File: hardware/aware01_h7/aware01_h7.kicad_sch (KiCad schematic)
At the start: 15 parts, among them U12 STM32H7B0ZBTx, U15 IS45S16800F-7TLA2, Y2 Crystal_GND24

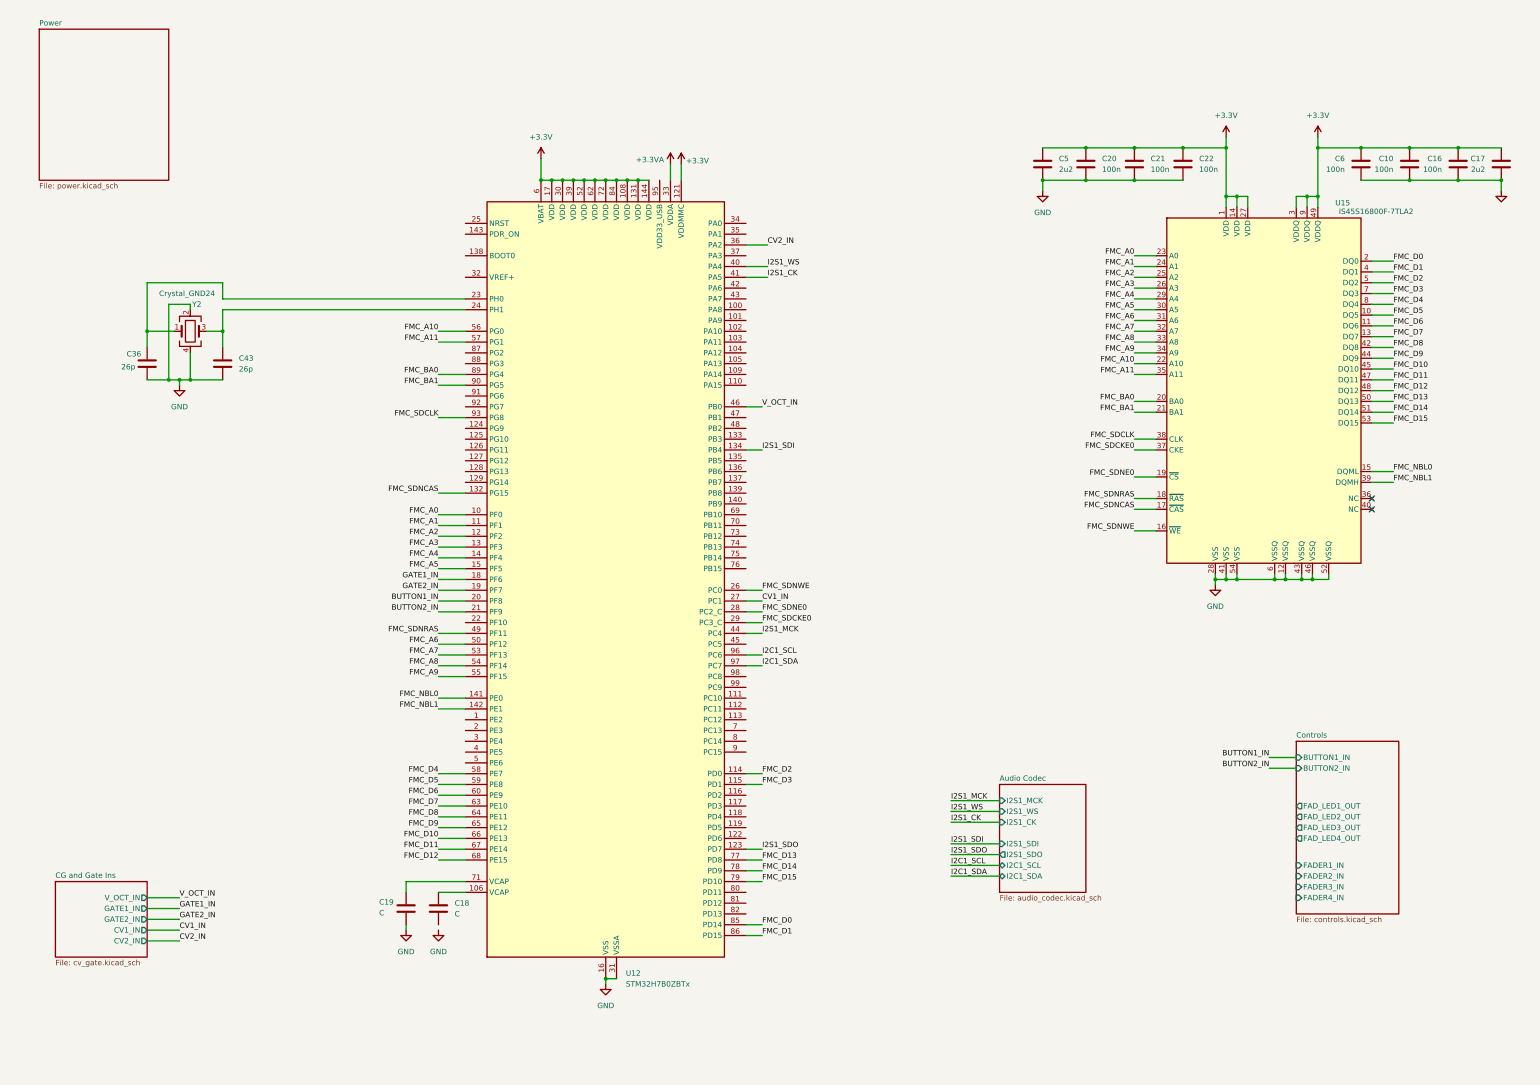
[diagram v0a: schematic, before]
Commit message: update schematic
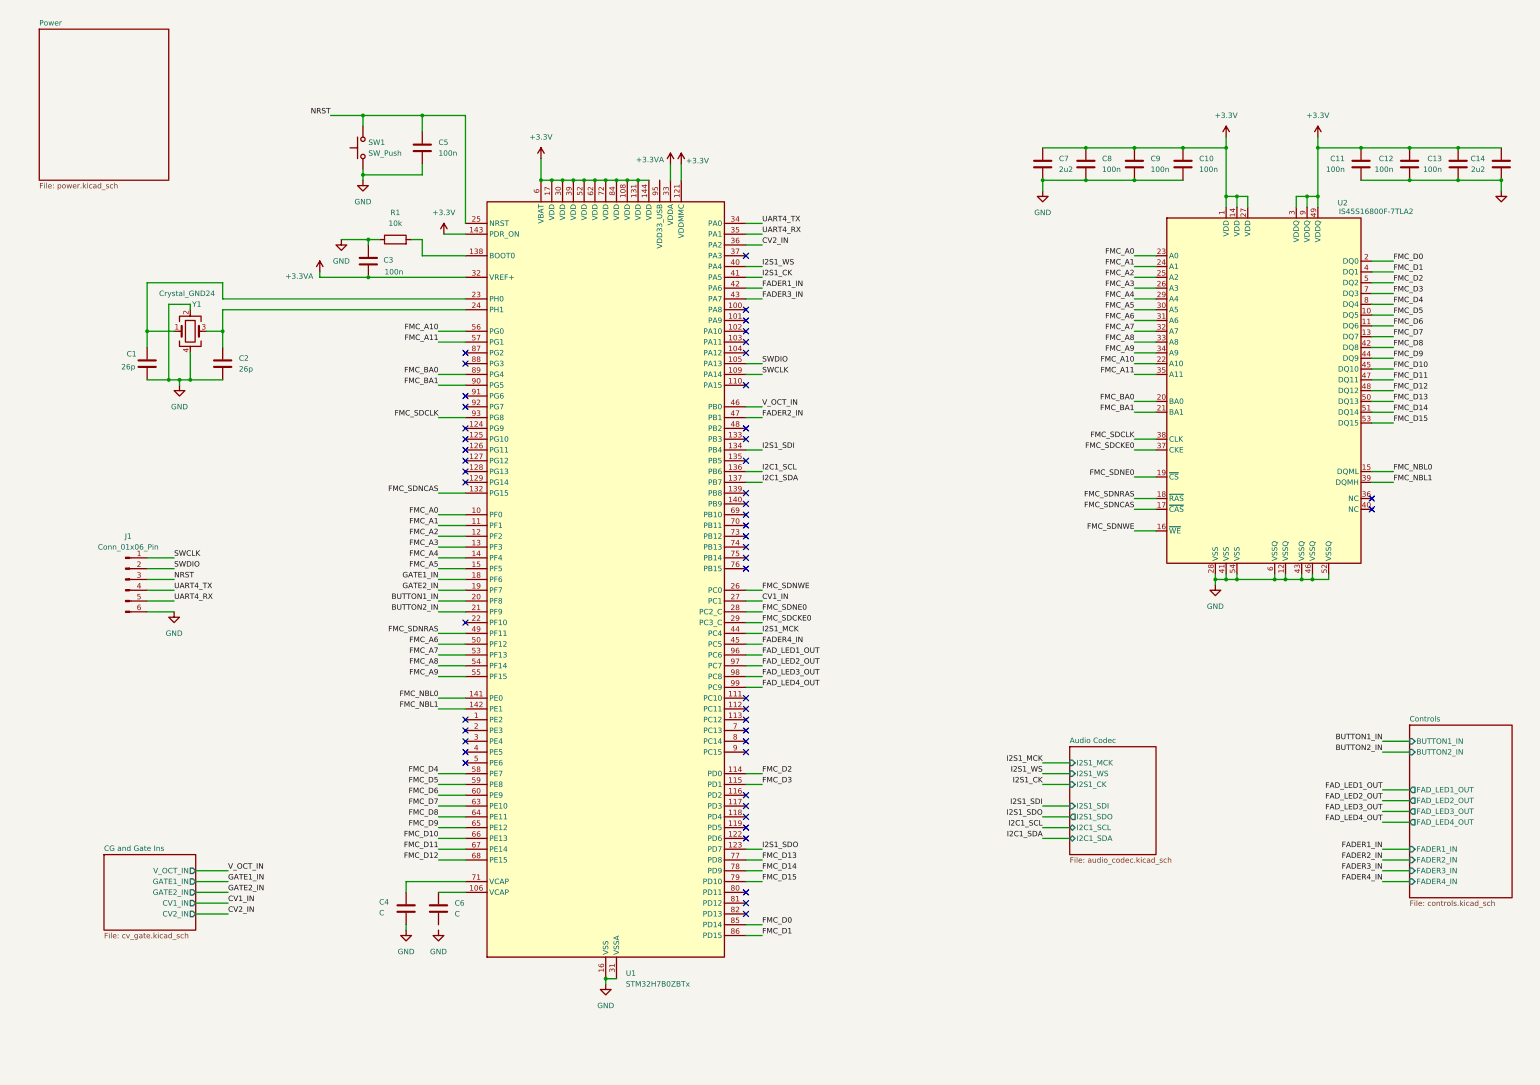
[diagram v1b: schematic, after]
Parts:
- added C3: 100n, symbol Device:C
- added C5: 100n, Capacitor_SMD:C_0201_0603Metric, symbol Device:C
- added J1: Conn_01x06_Pin, symbol Connector:Conn_01x06_Pin
- added R1: 10k, symbol Device:R
- added SW1: SW_Push, symbol Switch:SW_Push
- renumbered C36 to C1, C22 to C10, C6 to C11, C10 to C12, C16 to C13, C17 to C14, C43 to C2, C19 to C4, C18 to C6, C5 to C7, C20 to C8, C21 to C9, U12 to U1, U15 to U2, Y2 to Y1
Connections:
- net +3.3V: now also U1.143 (PDR_ON)
- net +3.3VA: now also U1.32 (VREF+), C3.2
- net GND: now also C3.1, C5.2, J1.6 (Pin_6), R1.1, SW1.1
- net I2C1_SCL: now also U1.136 (PB6); no longer U1.96 (PC6)
- net I2C1_SDA: now also U1.137 (PB7); no longer U1.97 (PC7)
- net SWDIO: now reaches U1.105 (PA13)
- net SWDIO: now also J1.2 (Pin_2)
- net SWCLK: now reaches U1.109 (PA14)
- net SWCLK: now also J1.1 (Pin_1)
- net at U1.138 (BOOT0): now also R1.2
- net NRST: now reaches U1.25 (NRST)
- net NRST: now also C5.1, J1.3 (Pin_3), SW1.2
- net UART4_TX: now reaches U1.34 (PA0)
- net UART4_TX: now also J1.4 (Pin_4)
- net UART4_RX: now reaches U1.35 (PA1)
- net UART4_RX: now also J1.5 (Pin_5)
- net FADER1_IN: now reaches U1.42 (PA6)
- net FADER3_IN: now reaches U1.43 (PA7)
- net FADER4_IN: now reaches U1.45 (PC5)
- net FADER2_IN: now reaches U1.47 (PB1)
- net FAD_LED3_OUT: now reaches U1.98 (PC8)
- net FAD_LED4_OUT: now reaches U1.99 (PC9)
- new net FAD_LED1_OUT: U1.96 (PC6)
- new net FAD_LED2_OUT: U1.97 (PC7)
- no-connect marks 2 -> 50

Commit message: refine schematic
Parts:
- C1, C10, C11, C12, C13, C2, C3, C8, C9: footprint (none) -> Capacitor_SMD:C_0603_1608Metric
- C14, C7: value 2u2 -> 2.2u; footprint (none) -> Capacitor_SMD:C_0603_1608Metric
- C4, C6: value C -> 100n; footprint (none) -> Capacitor_SMD:C_0603_1608Metric
- C5: footprint Capacitor_SMD:C_0201_0603Metric -> Capacitor_SMD:C_0603_1608Metric
- J1: footprint (none) -> Connector_PinHeader_2.54mm:PinHeader_1x06_P2.54mm_Vertical
- R1: footprint (none) -> Resistor_SMD:R_0603_1608Metric_Pad0.98x0.95mm_HandSolder
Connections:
- net +3.3V: now also J1.1 (Pin_1), U1.95 (VDD33_USB)
- net GND: now also C6.1
- net NRST: now also J1.5 (Pin_5); no longer J1.3 (Pin_3)
- net SWCLK: now also J1.2 (Pin_2); no longer J1.1 (Pin_1)
- net SWDIO: now also J1.3 (Pin_3); no longer J1.2 (Pin_2)
- net UART4_RX: no longer J1.5 (Pin_5)
- net UART4_TX: no longer J1.4 (Pin_4)
- new net SWO: J1.4 (Pin_4)
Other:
- note added: "BERECHNUNG?"
- note added: "TESTPADS EINBAUEN"
- note added: "TODO: SWO in CubeMX und an MCU in schematic hinzufügen"
- moved on the sheet: C3, C5, R1, SW1

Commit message: assign footprints
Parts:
- added H1, H2, H3, H4: MountingHole, MountingHole:MountingHole_2.2mm_M2_DIN965_Pad_TopOnly, symbol Mechanical:MountingHole
- added J2: Conn_01x03_Pin, symbol Connector:Conn_01x03_Pin
- C1, C2: value 26p -> 22p
- SW1: footprint (none) -> Button_Switch_SMD:SW_Push_1P1T_NO_CK_PTS125Sx43PSMTR
- U2: footprint Eurorack:SOP80P1176X120-54N -> Eurorack:IS45S16800F-7TLA2
- Y1: value Crystal_GND24 -> WE-XTAL 24.0MHz 50ppm; footprint (none) -> Crystal:Crystal_SMD_3225-4Pin_3.2x2.5mm_HandSoldering
- renumbered C5 to C4, C4 to C5
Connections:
- net GND: now also J2.3 (Pin_3)
- net SWO: now also U1.133 (PB3)
- net UART4_RX: now also J2.2 (Pin_2)
- net UART4_TX: now also J2.1 (Pin_1)
- no-connect marks 50 -> 47
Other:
- note removed: "BERECHNUNG?"
- moved on the sheet: C1, C2

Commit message: change jack symbols
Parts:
- J2: footprint (none) -> Connector:FanPinHeader_1x03_P2.54mm_Vertical
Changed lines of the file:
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@@
 			)
 		)
-		(property "Footprint" ""
+		(property "Footprint" "Connector:FanPinHeader_1x03_P2.54mm_Vertical"
 			(at 49.53 182.88 0)
 			(effects

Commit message: update pcb
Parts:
- removed H1, H2, H3, H4: MountingHole, MountingHole:MountingHole_2.2mm_M2_DIN965_Pad_TopOnly, symbol Mechanical:MountingHole
- added C61: 100n, Capacitor_SMD:C_0603_1608Metric, symbol Device:C
- C1, C2: Manufacturer_Name (none) -> KEMET; Manufacturer_Part_Number (none) -> C0603C220J1GACTU; Mouser Part Number (none) -> 80-C0603C220J1G
- C10, C11, C12, C13, C3, C4, C5, C6, C8, C9: Manufacturer_Name (none) -> KYOCERA AVX; Manufacturer_Part_Number (none) -> KAF15BR72A104KT; Mouser Part Number (none) -> 581-KAF15BR72A104KT
- C14, C7: Manufacturer_Name (none) -> Samsung Electro-Mechanics; Manufacturer_Part_Number (none) -> CL10A225KP8NNWC; Mouser Part Number (none) -> 187-CL10A225KP8NNWC
- J2: footprint Connector:FanPinHeader_1x03_P2.54mm_Vertical -> Connector_PinHeader_2.54mm:PinHeader_1x03_P2.54mm_Vertical
- SW1: footprint Button_Switch_SMD:SW_Push_1P1T_NO_CK_PTS125Sx43PSMTR -> Eurorack:TS046643BK100SMT; Manufacturer_Name (none) -> Same Sky; Manufacturer_Part_Number (none) -> TS04-66-43-BK-100-SMT; Mouser Part Number (none) -> 179-TS046643BK100SMT
- U1: Manufacturer_Name (none) -> STMicroelectronics; Manufacturer_Part_Number (none) -> STM32H7B0ZBT6; Mouser Part Number (none) -> 511-STM32H7B0ZBT6
- U2: footprint Eurorack:IS45S16800F-7TLA2 -> Eurorack:SOP80P1176X120-54N; Manufacturer_Name (none) -> ISSI; Manufacturer_Part_Number (none) -> IS45S16800F-7TLA2; Mouser Part Number (none) -> 870-IS45S16800F7TLA2
- Y1: Manufacturer_Name (none) -> Wurth Elektronik; Manufacturer_Part_Number (none) -> 830064703; Mouser Part Number (none) -> 710-830064703
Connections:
- net +3.3VA: now also C61.1
- net GND: now also C61.2

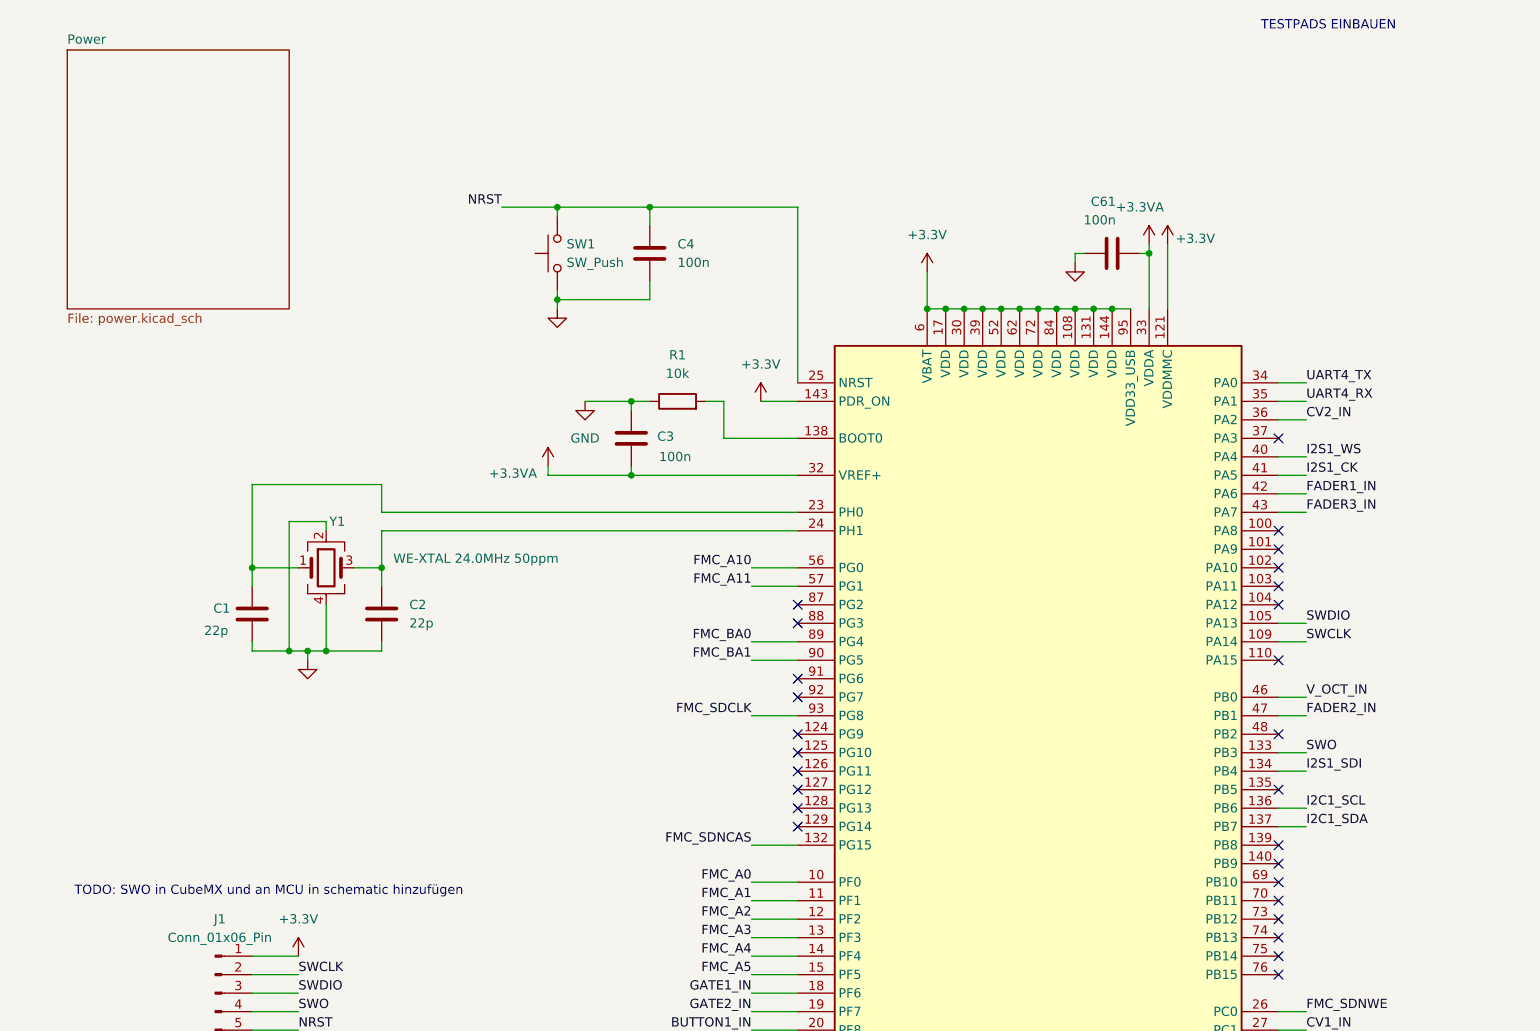
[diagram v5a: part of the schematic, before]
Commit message: change PWR to GND plane and reroute 3V3
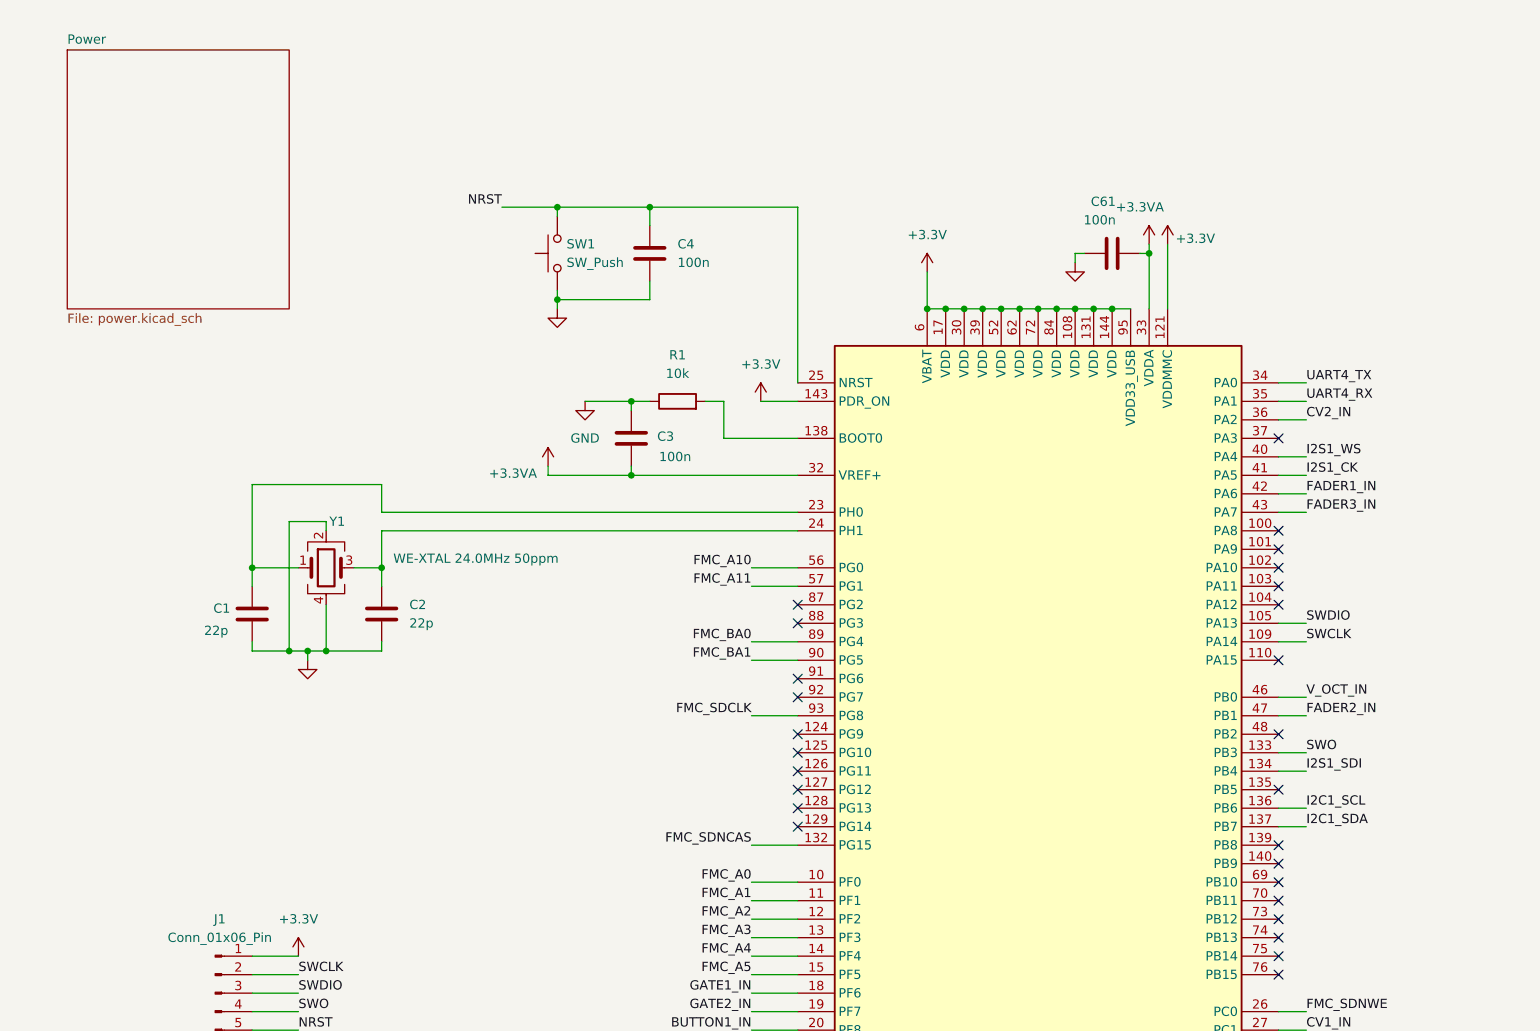
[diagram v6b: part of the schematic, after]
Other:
- note removed: "TESTPADS EINBAUEN"
- note removed: "TODO: SWO in CubeMX und an MCU in schematic hinzufügen"
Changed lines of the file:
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@@
-		)
-	)
-	(text "TESTPADS EINBAUEN"
-		(exclude_from_sim no)
-		(at 202.438 24.638 0)
-		(effects
-			(font
-				(size 1.27 1.27)
-			)
-		)
-	)
-	(text "TODO: SWO in CubeMX und an MCU in schematic hinzufügen"
-		(exclude_from_sim no)
-		(at 56.896 143.51 0)
-		(effects
-			(font
-				(size 1.27 1.27)
-			)
 		)
 	)
